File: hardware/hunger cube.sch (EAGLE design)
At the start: 32 parts, among them IC1 AVR-MEGA8-PPTH, T1 BPX81, T2 BPX81

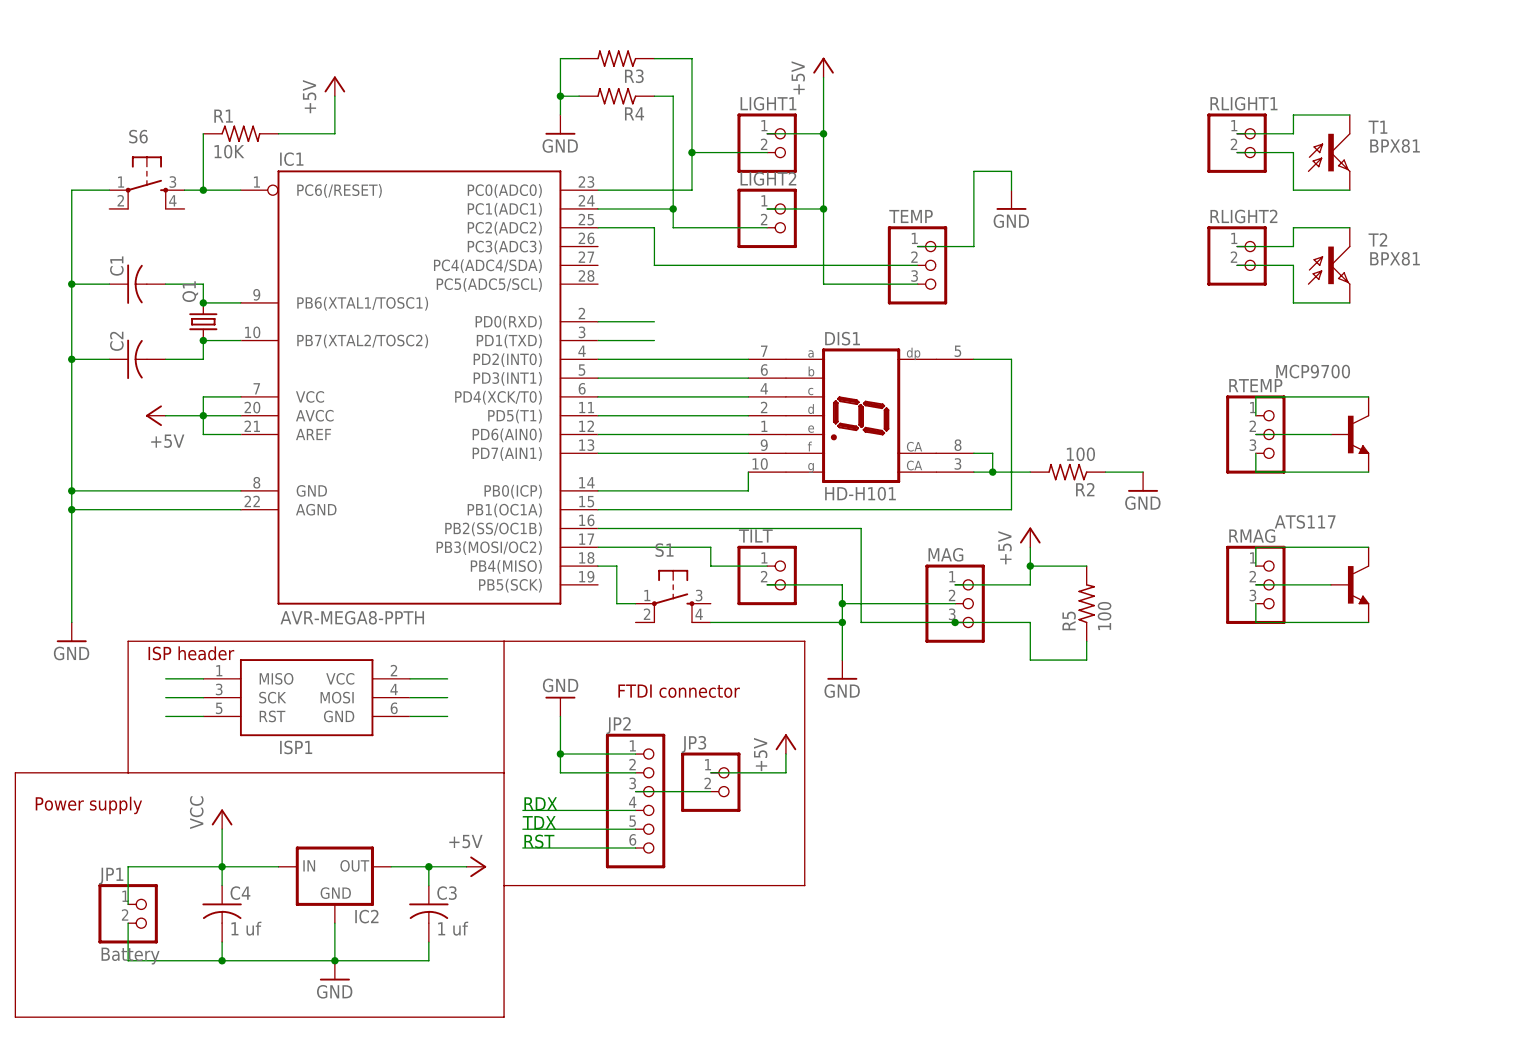
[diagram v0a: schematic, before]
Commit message: added custom parts for tilt sensor and the secret screw.  Laid out board for the first time.
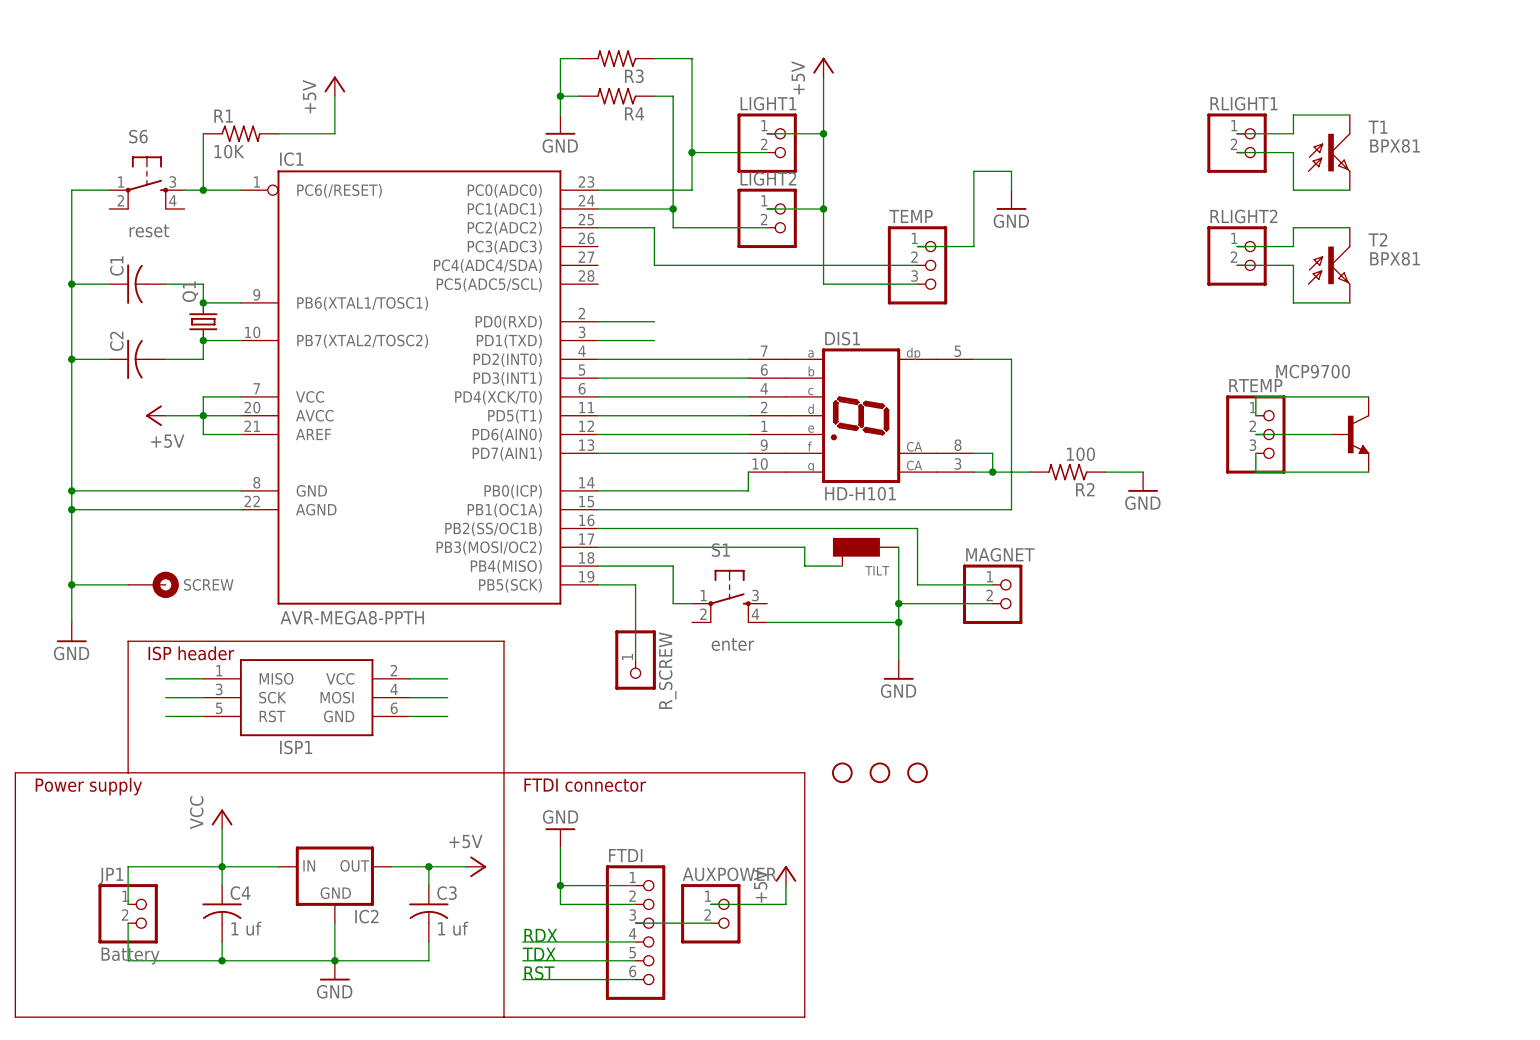
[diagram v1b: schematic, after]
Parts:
- removed ATS117: (no value), transistor:-NPN-TO92-EBC
- removed JP2: (no value), pinhead:PINHD-1X6
- removed JP3: (no value), pinhead:PINHD-1X2
- removed MAG, RMAG: (no value), pinhead:PINHD-1X3
- removed R5: 100, resistor:R-US_0207/12
- added AUXPOWER, MAGNET: (no value), pinhead:PINHD-1X2
- added FTDI: (no value), pinhead:PINHD-1X6
- added JP4, JP5, JP6: STAND-OFF, SparkFun:STAND-OFF
- added JP7: CONNECTED-SCREW-HOLE, connected-screw:CONNECTED-SCREW-HOLE
- added R_SCREW: (no value), pinhead:PINHD-1X1
- S1: value (none) -> enter
- S6: value (none) -> reset
- TILT: value (none) -> TILT-SENSOR; device pinhead:PINHD-1X2 -> tilt-sensor:TILT-SENSOR
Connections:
- removed net N$23: IC1.PB4(MISO), S1.1
- removed net N$24: IC1.PB3(MOSI/OC2), TILT.1
- removed net N$25: ATS117.C, RMAG.1
- removed net N$26: ATS117.E, RMAG.3
- removed net N$27: ATS117.B, RMAG.2
- net +5V: now also AUXPOWER.1; no longer JP3.1, MAG.1, R5.2
- net GND: now also FTDI.1, FTDI.2, JP7.SCREW, MAGNET.2, TILT.CENTER; no longer JP2.1, JP2.2, MAG.2, TILT.2
- net MISO: now also IC1.PB4(MISO), S1.1
- net MOSI: now also IC1.PB3(MOSI/OC2), TILT.SLEEVE
- net N$18: now also MAGNET.1; no longer MAG.3, R5.1
- net N$5: now also AUXPOWER.2, FTDI.3; no longer JP2.3, JP3.2
- net RDX: now also FTDI.4; no longer JP2.4
- net RST: now also FTDI.6; no longer JP2.6
- net SCK: now also IC1.PB5(SCK), R_SCREW.1
- net TDX: now also FTDI.5; no longer JP2.5
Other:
- moved on the sheet: S1

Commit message: 
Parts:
- removed AUXPOWER, LIGHT1, LIGHT2, MAGNET: (no value), pinhead:PINHD-1X2
- removed FTDI: (no value), pinhead:PINHD-1X6
- removed TEMP: (no value), pinhead:PINHD-1X3
- added JP14: D0-D1, pinhead:PINHD-1X2
- added JP2: Light1, pinhead:PINHD-1X2
- added JP3: Light 2, pinhead:PINHD-1X2
- added JP8: TEMP, pinhead:PINHD-1X3
- added JP9: Magnet, pinhead:PINHD-1X2
- added SG1: BUZZERPTH, SparkFun:BUZZERPTH
- added ST1, ST2, ST3: STAND-OFF, SparkFun:STAND-OFF
- JP10: value (none) -> R Light 1
- JP11: value (none) -> R light 2
- JP12: value (none) -> R temp
- JP13: value (none) -> R screw
- JP4: value STAND-OFF -> FTDI; device SparkFun:STAND-OFF -> pinhead:PINHD-1X6
- JP5: value STAND-OFF -> Aux Pwr; device SparkFun:STAND-OFF -> pinhead:PINHD-1X2
- JP6: value STAND-OFF -> A4-A5; device SparkFun:STAND-OFF -> pinhead:PINHD-1X2
- JP7: value CONNECTED-SCREW-HOLE -> Connected screw hole
- renumbered RLIGHT1 to JP10, RLIGHT2 to JP11, RTEMP to JP12, R_SCREW to JP13
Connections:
- new net N$23: IC1.PB2(SS/OC1B), SG1.1
- new net N$24: IC1.PC4(ADC4/SDA), JP6.1
- new net N$25: IC1.PC5(ADC5/SCL), JP6.2
- net +5V: now also JP2.1, JP3.1, JP5.1, JP8.3; no longer AUXPOWER.1, LIGHT1.1, LIGHT2.1, TEMP.3
- net GND: now also JP4.1, JP4.2, JP8.1, JP9.1, S1.3, SG1.2; no longer FTDI.1, FTDI.2, MAGNET.2, TEMP.1
- net LIGHT2: now also JP2.2; no longer LIGHT1.2
- net MISO: now also S1.2
- net N$14: now also JP3.2; no longer LIGHT2.2
- net N$18: now also IC1.PC3(ADC3), JP9.2; no longer IC1.PB2(SS/OC1B), MAGNET.1
- net N$19: now also JP8.2; no longer TEMP.2
- net N$5: now also JP4.3, JP5.2; no longer AUXPOWER.2, FTDI.3
- net RDX: now also JP14.1, JP4.4; no longer FTDI.4
- net RST: now also JP4.6; no longer FTDI.6
- net TDX: now also JP14.2, JP4.5; no longer FTDI.5

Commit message: Added box svg to archive, measured dimentions of parts of board for box, and tweaked where some holes are.
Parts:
- C1, C2: value (none) -> 18pF
- IC2: value (none) -> LDO 5v
- JP14: value D0-D1 -> D0 D1
- JP6: value A4-A5 -> A5 A4
- MCP9700: value (none) -> temp
- Q1: value (none) -> 16Mhz
- T1, T2: value BPX81 -> PT204
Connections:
- net LIGHT2 renamed A0-LIGHT1
- net MISO renamed D12-MISO-ENTER
- net MOSI renamed D11-MOSI-TILT
- net N$1 renamed D2-SEGA
- net N$10 renamed D8-SEGG
- net N$11 renamed D9-DP
- net N$14 renamed A1-LIGHT2
- net N$18 renamed A3-MAGNET
- net N$19 renamed A2-TEMP
- net N$2 renamed D3-SEBB
- net N$23 renamed D10-BUZZER
- net N$24 renamed A4
- net N$25 renamed A5
- net N$6 renamed D4-SEGC
- net N$7 renamed D5-SEGD
- net N$8 renamed D6-SEGE
- net N$9 renamed D7-SEGF
- net RDX renamed D0-RDX
- net SCK renamed D13-SCK-SCREW
- net TDX renamed D1-TDX
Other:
- note added: "Remote Daughterboards"
- moved on the sheet: JP10, JP11, JP12, MCP9700, T1, T2

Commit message: 
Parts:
- added C5: .1 uf, resistor:C-US025-050X050
- DIS1: value HD-H101 -> display
- T1: value PT204 -> light
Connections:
- net N$12 renamed DSP-GND
- new net N$1: C5.2, JP4.6
- net RST: now also C5.1; no longer JP4.6
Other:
- moved on the sheet: JP4, JP5
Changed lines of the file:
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@@
 <part name="C1" library="resistor" deviceset="C-US" device="025-050X050" value="18pF"/>
 <part name="C2" library="resistor" deviceset="C-US" device="025-050X050" value="18pF"/>
-<part name="DIS1" library="display-hp" deviceset="HD-H101" device=""/>
+<part name="DIS1" library="display-hp" deviceset="HD-H101" device="" value="display"/>
 <part name="IC2" library="adafruit" deviceset="MCP1700" device="INLINE" value="LDO 5v"/>
 <part name="C3" library="resistor" deviceset="C-US" device="025-050X050" value="1 uf"/>
@@
 <part name="JP10" library="pinhead" deviceset="PINHD-1X2" device="" value="R Light 1"/>
 <part name="JP11" library="pinhead" deviceset="PINHD-1X2" device="" value="R light 2"/>
-<part name="T1" library="opto-trans-siemens" deviceset="BPX81" device="" value="PT204"/>
+<part name="T1" library="opto-trans-siemens" deviceset="BPX81" device="" value="light"/>
 <part name="T2" library="opto-trans-siemens" deviceset="BPX81" device="" value="PT204"/>
 <part name="MCP9700" library="transistor" deviceset="*-NPN-" device="TO92-EBC" value="temp"/>
@@
 <part name="JP6" library="pinhead" deviceset="PINHD-1X2" device="" value="A5 A4"/>
 <part name="JP14" library="pinhead" deviceset="PINHD-1X2" device="" value="D0 D1"/>
+<part name="C5" library="resistor" deviceset="C-US" device="025-050X050" value=".1 uf"/>
 </parts>
 <sheets>
 <sheet>
 <plain>
-<text x="35.56" y="-45.72" size="1.778" layer="91">RDX</text>
-<text x="35.56" y="-48.26" size="1.778" layer="91">TDX</text>
-<text x="35.56" y="-50.8" size="1.778" layer="91">RST</text>
+<text x="43.18" y="-45.72" size="1.778" layer="91">RDX</text>
+<text x="43.18" y="-48.26" size="1.778" layer="91">TDX</text>
+<text x="34.036" y="-36.068" size="1.778" layer="91">RST</text>
 <wire x1="-33.02" y1="-22.86" x2="-17.78" y2="-22.86" width="0.1524" layer="94"/>
 <wire x1="33.02" y1="-22.86" x2="33.02" y2="-55.88" width="0.1524" layer="94"/>
@@
 <instance part="P+3" gate="1" x="10.16" y="71.12"/>
 <instance part="P+4" gate="1" x="-15.24" y="25.4" rot="R90"/>
-<instance part="JP4" gate="A" x="53.34" y="-45.72"/>
+<instance part="JP4" gate="A" x="55.88" y="-45.72"/>
 <instance part="GND3" gate="1" x="40.64" y="-30.48" rot="R180"/>
 <instance part="P+5" gate="1" x="71.12" y="-33.02"/>
-<instance part="JP5" gate="G$1" x="63.5" y="-43.18"/>
+<instance part="JP5" gate="G$1" x="66.04" y="-43.18"/>
 <instance part="GND4" gate="1" x="119.38" y="15.24"/>
 <instance part="JP2" gate="G$1" x="68.58" y="68.58" smashed="yes">
@@
 <attribute name="VALUE" x="118.11" y="33.02" size="1.778" layer="96"/>
 </instance>
+<instance part="C5" gate="G$1" x="35.56" y="-43.18"/>
 </instances>
 <busses>
@@
 <pinref part="JP4" gate="A" pin="1"/>
 <pinref part="GND3" gate="1" pin="GND"/>
-<wire x1="50.8" y1="-38.1" x2="40.64" y2="-38.1" width="0.1524" layer="91"/>
+<wire x1="53.34" y1="-38.1" x2="40.64" y2="-38.1" width="0.1524" layer="91"/>
 <wire x1="40.64" y1="-38.1" x2="40.64" y2="-33.02" width="0.1524" layer="91"/>
 <pinref part="JP4" gate="A" pin="2"/>
-<wire x1="50.8" y1="-40.64" x2="40.64" y2="-40.64" width="0.1524" layer="91"/>
+<wire x1="53.34" y1="-40.64" x2="40.64" y2="-40.64" width="0.1524" layer="91"/>
 <wire x1="40.64" y1="-40.64" x2="40.64" y2="-38.1" width="0.1524" layer="91"/>
 <junction x="40.64" y="-38.1"/>
@@
 <pinref part="JP5" gate="G$1" pin="1"/>
 <pinref part="P+5" gate="1" pin="+5V"/>
-<wire x1="60.96" y1="-40.64" x2="71.12" y2="-40.64" width="0.1524" layer="91"/>
+<wire x1="63.5" y1="-40.64" x2="71.12" y2="-40.64" width="0.1524" layer="91"/>
 <wire x1="71.12" y1="-40.64" x2="71.12" y2="-35.56" width="0.1524" layer="91"/>
 </segment>
@@
 </segment>
 <segment>
-<pinref part="JP4" gate="A" pin="6"/>
-<wire x1="50.8" y1="-50.8" x2="35.56" y2="-50.8" width="0.1524" layer="91"/>
+<pinref part="C5" gate="G$1" pin="1"/>
+<wire x1="35.56" y1="-40.64" x2="35.56" y2="-38.1" width="0.1524" layer="91"/>
 </segment>
 </net>
@@
 <pinref part="JP4" gate="A" pin="3"/>
 <pinref part="JP5" gate="G$1" pin="2"/>
-<wire x1="50.8" y1="-43.18" x2="60.96" y2="-43.18" width="0.1524" layer="91"/>
+<wire x1="53.34" y1="-43.18" x2="63.5" y2="-43.18" width="0.1524" layer="91"/>
 </segment>
 </net>
@@
 <segment>
 <pinref part="JP4" gate="A" pin="4"/>
-<wire x1="50.8" y1="-45.72" x2="35.56" y2="-45.72" width="0.1524" layer="91"/>
+<wire x1="53.34" y1="-45.72" x2="43.18" y2="-45.72" width="0.1524" layer="91"/>
 </segment>
 <segment>
@@
 <segment>
 <pinref part="JP4" gate="A" pin="5"/>
-<wire x1="50.8" y1="-48.26" x2="35.56" y2="-48.26" width="0.1524" layer="91"/>
+<wire x1="53.34" y1="-48.26" x2="43.18" y2="-48.26" width="0.1524" layer="91"/>
 </segment>
 </net>
@@
 </segment>
 </net>
-<net name="N$12" class="0">
+<net name="DSP-GND" class="0">
 <segment>
 <pinref part="DIS1" gate="M" pin="CA@1"/>
@@
 </segment>
 </net>
+<net name="N$1" class="0">
+<segment>
+<pinref part="JP4" gate="A" pin="6"/>
+<pinref part="C5" gate="G$1" pin="2"/>
+<wire x1="53.34" y1="-50.8" x2="35.56" y2="-50.8" width="0.1524" layer="91"/>
+<wire x1="35.56" y1="-50.8" x2="35.56" y2="-48.26" width="0.1524" layer="91"/>
+</segment>
+</net>

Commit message: 
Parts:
- added D1: (no value), adafruit:SCHOTTKY-DIODEDO41
- SG1: value BUZZERPTH -> F/CM12P; device SparkFun:BUZZERPTH -> buzzer:F/CM12P
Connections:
- new net N$2: D1.A, JP1.1
- net VCC: now also D1.C; no longer JP1.1
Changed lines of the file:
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@@
 <part name="JP13" library="pinhead" deviceset="PINHD-1X1" device="" value="R screw"/>
 <part name="TILT" library="tilt-sensor" deviceset="TILT-SENSOR" device=""/>
-<part name="SG1" library="SparkFun" deviceset="BUZZER" device="PTH"/>
+<part name="SG1" library="buzzer" deviceset="F/CM12P" device=""/>
 <part name="JP6" library="pinhead" deviceset="PINHD-1X2" device="" value="A5 A4"/>
 <part name="JP14" library="pinhead" deviceset="PINHD-1X2" device="" value="D0 D1"/>
 <part name="C5" library="resistor" deviceset="C-US" device="025-050X050" value=".1 uf"/>
+<part name="D1" library="adafruit" deviceset="SCHOTTKY-DIODE" device="DO41"/>
 </parts>
 <sheets>
@@
 <instance part="JP13" gate="G$1" x="50.8" y="-10.16" rot="R270"/>
 <instance part="TILT" gate="G$1" x="81.28" y="7.62" rot="R180"/>
-<instance part="SG1" gate="G$1" x="96.52" y="5.08"/>
+<instance part="SG1" gate="G$1" x="96.52" y="2.54"/>
 <instance part="JP6" gate="G$1" x="116.84" y="45.72" smashed="yes">
 <attribute name="NAME" x="110.49" y="51.435" size="1.778" layer="95"/>
@@
 </instance>
 <instance part="C5" gate="G$1" x="35.56" y="-43.18"/>
+<instance part="D1" gate="G$1" x="-12.7" y="-33.02"/>
 </instances>
 <busses>
@@
 <wire x1="-5.08" y1="-38.1" x2="-5.08" y2="-35.56" width="0.1524" layer="91"/>
 <junction x="-5.08" y="-35.56"/>
-<pinref part="JP1" gate="G$1" pin="1"/>
-<wire x1="-17.78" y1="-40.64" x2="-17.78" y2="-35.56" width="0.1524" layer="91"/>
-<wire x1="-17.78" y1="-35.56" x2="-5.08" y2="-35.56" width="0.1524" layer="91"/>
+<pinref part="D1" gate="G$1" pin="C"/>
+<wire x1="-10.16" y1="-33.02" x2="-7.62" y2="-33.02" width="0.1524" layer="91"/>
+<wire x1="-7.62" y1="-33.02" x2="-7.62" y2="-35.56" width="0.1524" layer="91"/>
+<wire x1="-7.62" y1="-35.56" x2="-5.08" y2="-35.56" width="0.1524" layer="91"/>
 </segment>
 </net>
@@
 <pinref part="SG1" gate="G$1" pin="2"/>
 <wire x1="71.12" y1="-2.54" x2="86.36" y2="-2.54" width="0.1524" layer="91"/>
-<wire x1="99.06" y1="2.54" x2="99.06" y2="-2.54" width="0.1524" layer="91"/>
-<wire x1="99.06" y1="-2.54" x2="86.36" y2="-2.54" width="0.1524" layer="91"/>
+<wire x1="101.6" y1="0" x2="101.6" y2="-2.54" width="0.1524" layer="91"/>
+<wire x1="101.6" y1="-2.54" x2="86.36" y2="-2.54" width="0.1524" layer="91"/>
 <pinref part="S1" gate="S" pin="3"/>
 <wire x1="68.58" y1="0" x2="71.12" y2="0" width="0.1524" layer="91"/>
@@
 <wire x1="91.44" y1="10.16" x2="91.44" y2="0" width="0.1524" layer="91"/>
 <pinref part="SG1" gate="G$1" pin="1"/>
-<wire x1="91.44" y1="0" x2="96.52" y2="0" width="0.1524" layer="91"/>
-<wire x1="96.52" y1="0" x2="96.52" y2="2.54" width="0.1524" layer="91"/>
+<wire x1="91.44" y1="0" x2="93.98" y2="0" width="0.1524" layer="91"/>
 </segment>
 </net>
@@
 </segment>
 </net>
+<net name="N$2" class="0">
+<segment>
+<pinref part="JP1" gate="G$1" pin="1"/>
+<wire x1="-17.78" y1="-40.64" x2="-17.78" y2="-33.02" width="0.1524" layer="91"/>
+<pinref part="D1" gate="G$1" pin="A"/>
+<wire x1="-17.78" y1="-33.02" x2="-15.24" y2="-33.02" width="0.1524" layer="91"/>
+</segment>
+</net>
